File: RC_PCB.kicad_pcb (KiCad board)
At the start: 2 copper layers, 19 parts, among them SW1 SW_Push, SW2 SW_Push, SW3 SW_Push, SW4 SW_Push, U1 RFM9x, U2 Teensy4.0, U3 128x64_OLED, U4 Joystick, U5 Joystick

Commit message: fixed lcd footprint
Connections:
- U3 pad 6: +3V3 -> unconnected-(U3-Pad6)

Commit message: initial layout complete
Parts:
- added C6: 0.1uF, Capacitor_SMD:C_0805_2012Metric_Pad1.18x1.45mm_HandSolder, F.Cu at (111.8, 63.5)
- added C7: 0.1uF, Capacitor_SMD:C_0805_2012Metric_Pad1.18x1.45mm_HandSolder, F.Cu at (181.6, 97.8)
- added H3: MountingHole, MountingHole:MountingHole_3.2mm_M3, F.Cu at (200.7, 53.3)
- added H3: MountingHole, MountingHole:MountingHole_3.2mm_M3, F.Cu at (111.8, 127.0)
- added H3: MountingHole, MountingHole:MountingHole_3.2mm_M3, F.Cu at (111.8, 53.3)
- added H3: MountingHole, MountingHole:MountingHole_3.2mm_M3, F.Cu at (200.7, 127.0)
- added R5: 10k, Resistor_SMD:R_0805_2012Metric_Pad1.20x1.40mm_HandSolder, F.Cu at (121.9, 59.7)
- added R6: 10k, Resistor_SMD:R_0805_2012Metric_Pad1.20x1.40mm_HandSolder, F.Cu at (177.5, 97.8)
- moved C2 93.8 mm to (177.8, 68.6), turned to 90 degrees
- moved C3 92.2 mm to (185.4, 68.6), turned to 90 degrees
- moved C1 89.5 mm to (172.7, 54.6), turned to 90 degrees
- moved JT1 85.2 mm to (165.1, 52.1)
- moved C5 77.8 mm to (172.7, 82.5), turned to 90 degrees
- moved C4 74.6 mm to (157.5, 52.3), turned to -90 degrees
- moved SW2 43.0 mm to (161.4, 67.3)
- moved U4 39.7 mm to (120.7, 76.2)
- moved SW3 29.6 mm to (189.3, 67.3)
- moved R3 29.6 mm to (185.4, 72.4)
- moved R2 24.7 mm to (177.8, 72.4), turned to 180 degrees
- moved U3 20.3 mm to (158.2, 125.4)
- moved U1 19.0 mm to (110.5, 116.8), turned to 90 degrees
- moved U2 16.3 mm to (147.3, 68.6)
- moved R1 14.8 mm to (172.7, 58.4)
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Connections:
- U4 pad B1B: (no net) -> /JOY_LEFT_BTN
- U4 pad B2B: (no net) -> GND
- U5 pad B1B: (no net) -> /JOY_RIGHT_BTN
- U5 pad B2B: (no net) -> GND
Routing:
- net GND: track 0.00 -> 449.0 mm, vias 0 -> 3
- net +3V3: track 0.00 -> 263.3 mm, vias 0 -> 2
- net /JOY_RIGHT_H: track 0.00 -> 116.6 mm
- net /JOY_RIGHT_BTN: track 0.00 -> 76.6 mm, vias 0 -> 3
- net /JOY_RIGHT_V: track 0.00 -> 74.2 mm, vias 0 -> 2
- net /BTN_RIGHT: track 0.00 -> 58.2 mm
- net /BTN_DOWN: track 0.00 -> 53.2 mm
- net /JOY_LEFT_V: track 0.00 -> 48.1 mm
- net /BTN_UP: track 0.00 -> 43.0 mm
- net /JOY_LEFT_H: track 0.00 -> 37.1 mm, vias 0 -> 1
- net /LORA_INT: track 0.00 -> 36.9 mm
- net /JOY_LEFT_BTN: track 0.00 -> 35.6 mm
- net /OLED_SCL: track 0.00 -> 33.2 mm
- net /LORA_SCK: track 0.00 -> 31.0 mm, vias 0 -> 1
- net /OLED_SDA: track 0.00 -> 30.8 mm
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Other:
- board outline added: 99.1 x 83.8 mm

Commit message: completed drc, added amp logo, generated gerbers
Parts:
- added U2: Logo, AMP:Logo, F.Cu at (163.6, 94.5)

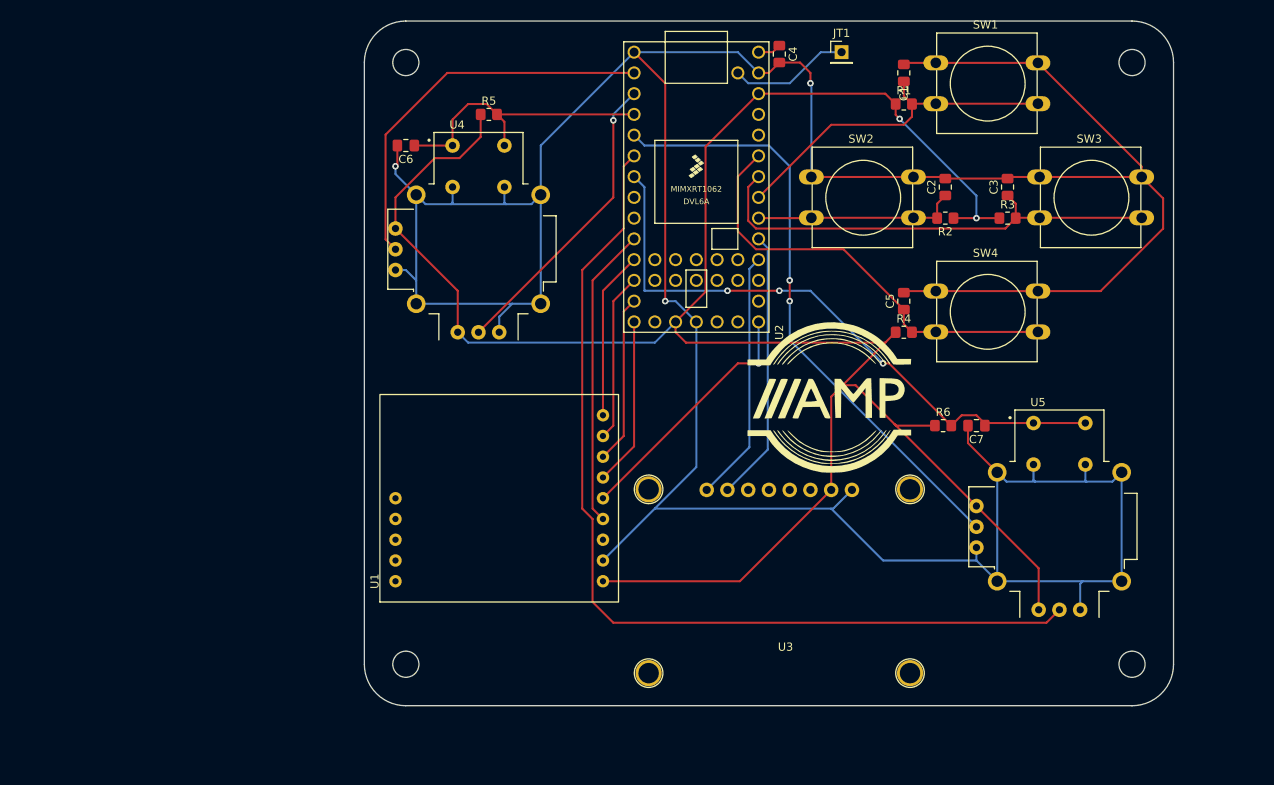
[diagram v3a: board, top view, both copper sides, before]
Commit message: updated oled footprint
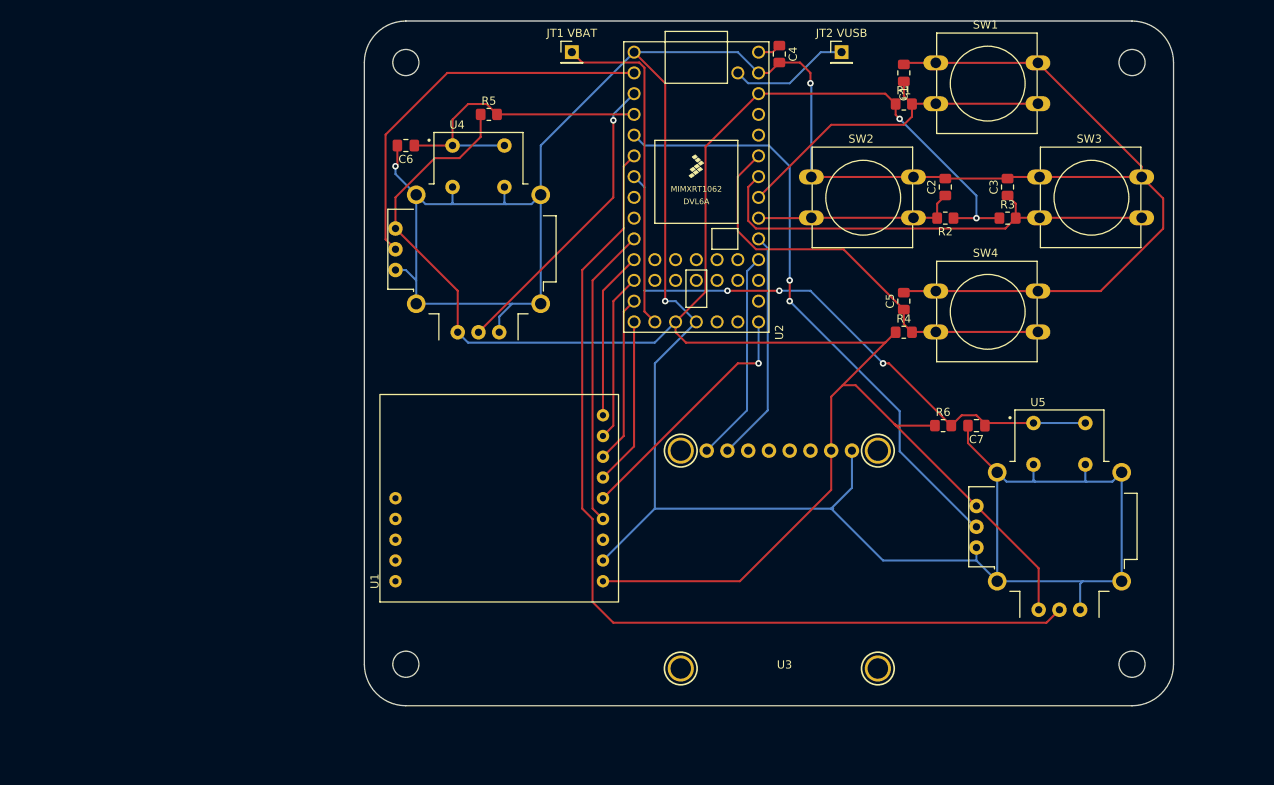
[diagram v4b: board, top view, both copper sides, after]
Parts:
- added JT1 VBAT: Conn_01x01_Male, Connector_PinHeader_2.54mm:PinHeader_1x01_P2.54mm_Vertical, F.Cu at (132.1, 52.1)
- JT2 VUSB: renamed from JT1
- U2: moved to B.Cu
- moved U2 23.2 mm to (157.5, 116.8), turned to 180 degrees
- moved U3 5.26 mm to (160.7, 130.1)
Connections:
- U2 pad 15: unconnected-(U2-Pad15) -> Net-(JT1-Pad1)
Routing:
- net Net-(JT1-Pad1): track 0.00 -> 41.3 mm
- net GND: track 449.0 -> 453.9 mm
- net /OLED_SDA: track 30.8 -> 26.0 mm
- net /OLED_SCL: track 33.2 -> 28.4 mm
- net /JOY_LEFT_BTN: track 35.6 -> 37.7 mm
